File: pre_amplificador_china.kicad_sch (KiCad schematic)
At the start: 28 parts, among them J1 Conn_01x02, J2 Conn_01x02, J202 Conn_01x04, K301 ADW11, Q301 BSS138, Q302 BSS138, SW1 SW_Push_Dual, U106 LM7805_TO220, U202 HT66F0175_185

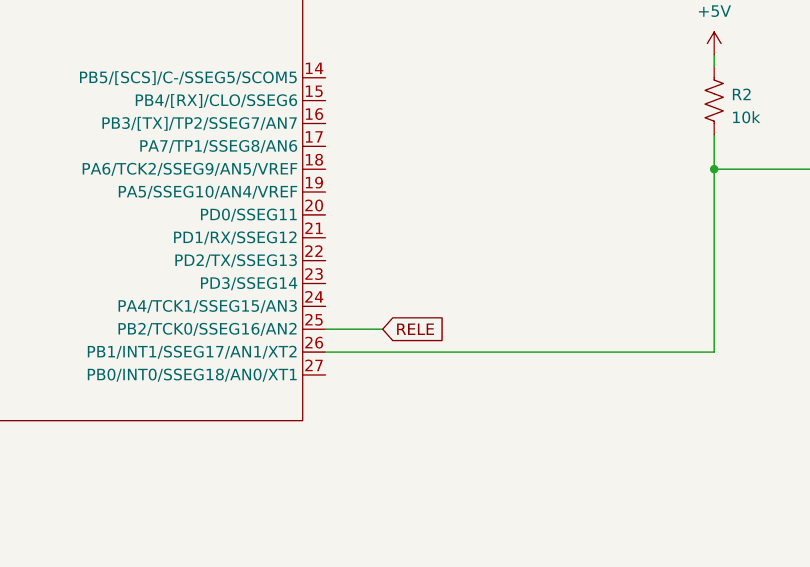
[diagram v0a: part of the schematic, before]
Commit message: correcao de standby no IC
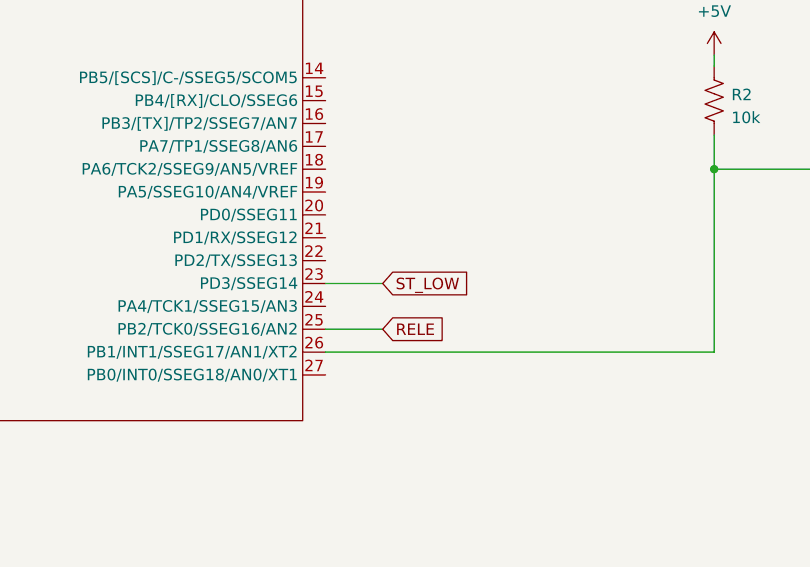
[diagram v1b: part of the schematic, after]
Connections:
- net ST_LOW: now reaches U202.23 (PD3/SSEG14)
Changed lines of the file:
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@@
+	(wire
+		(pts
+			(xy 139.7 123.19) (xy 133.35 123.19)
+		)
+		(stroke
+			(width 0)
+			(type default)
+		)
+	)
 	(wire
 		(pts
@@
 				(hide yes)
 			)
+		)
+	)
+	(global_label "ST_LOW"
+		(shape input)
+		(at 139.7 123.19 0)
+		(fields_autoplaced yes)
+		(effects
+			(font
+				(size 1.27 1.27)
+			)
+			(justify left)
+		)
+		(property "Intersheetrefs" "${INTERSHEET_REFS}"
+			(at 149.6399 123.19 0)
+			(effects
+				(font
+					(size 1.27 1.27)
+				)
+				(justify left)
+				(hide yes)
+			)

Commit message: v2.0 pre APL_STA2150
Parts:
- removed D1: LED, LED_THT:LED_D3.0mm_Clear, symbol Device:LED
- removed H4: MountingHole, MountingHole:MountingHole_3.5mm, symbol Mechanical:MountingHole
- removed SW1: SW_Push_Dual, Library:ButtonLoud, symbol Switch:SW_Push_Dual
- added SW1: SW_Push, Library:Button, symbol Switch:SW_Push
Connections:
- net GND: now also SW1.2
- net ST_OUT: now reaches R205.2
- net at K301.3: now also J1.2 (Pin_2); no longer J1.1 (Pin_1)
- net at K301.5: now also J1.1 (Pin_1); no longer J1.2 (Pin_2)
- net at R2.1, U202.26 (PB1/INT1/SSEG17/AN1/XT2): now also SW1.1
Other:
- moved on the sheet: J1
